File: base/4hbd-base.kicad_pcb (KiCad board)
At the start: 2 copper layers, 150 x 100 mm, 198 parts, among them J1 Screw_Terminal_01x03, J10 Conn_01x08, J12 Spring_Terminal_Connector_01x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, J14 Screw_Terminal_01x02, J15 Conn_01x27, J16 Conn_01x27, J2 Screw_Terminal_01x03, J3 Screw_Terminal_01x03, J4 Screw_Terminal_01x03, J5 Screw_Terminal_01x02, J6 Screw_Terminal_01x02, J7 Screw_Terminal_01x02, J8 Screw_Terminal_01x02, J9 Screw_Terminal_01x04, Q1 irf540n, Q10 2N7002, Q11 2N7002, Q12 IRLML2060TRPBF, Q2 irf540n, Q3 irf540n, Q4 irf540n, Q5 irf540n, Q6 irf540n, Q7 irf540n, Q8 irf540n, U1 SI8640, U11 MOCD217M, U12 MOCD217M, U13 MOCD217M, U14 AMS1117-5.0, U15 AMS1117-5.0, U16 LM2596S-ADJ, U17 AM26LV32, U18 LM2596S-ADJ, U19 AMS1117-5.0, U2 SI8640, U3 IR25606, U4 IR25606, U5 IR25606, U6 IR25606, U7 ACS712xLCTR-30A, U8 ACS712xLCTR-30A

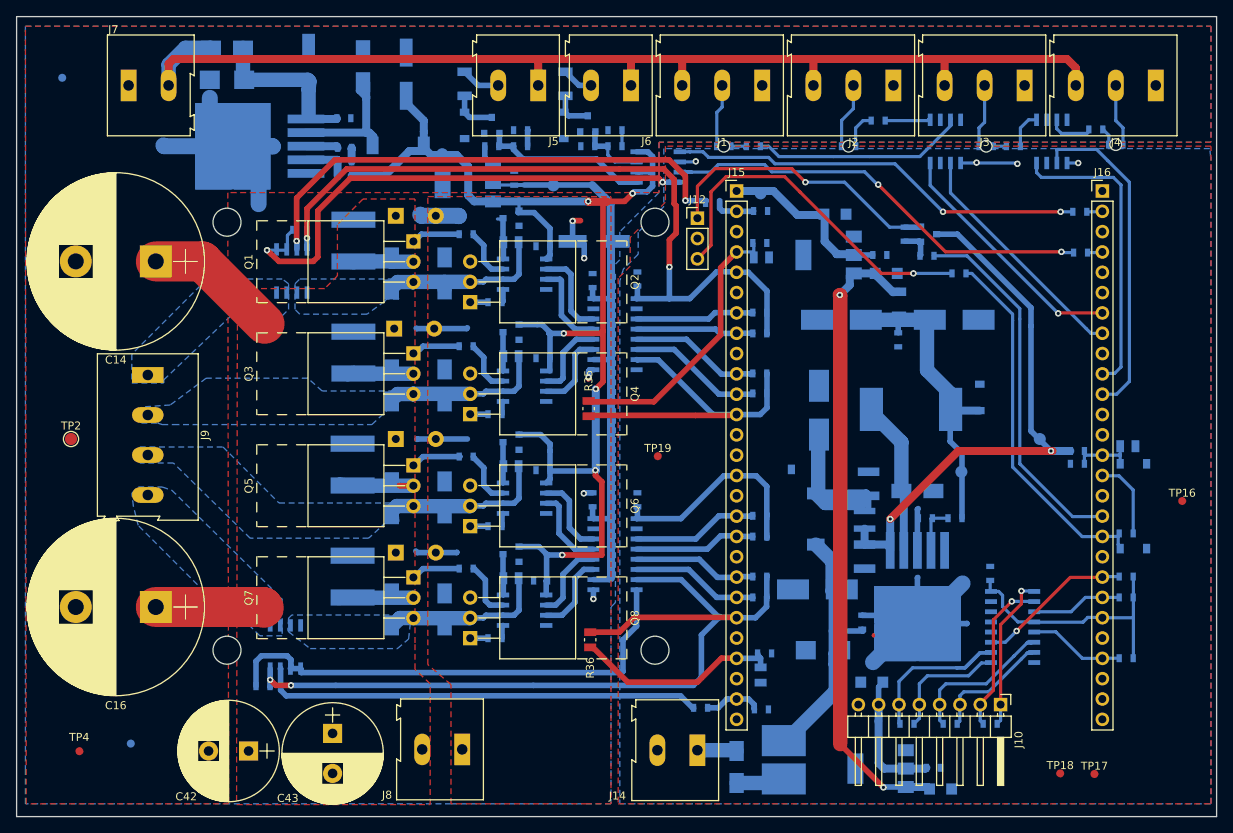
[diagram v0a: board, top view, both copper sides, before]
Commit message: add power vias
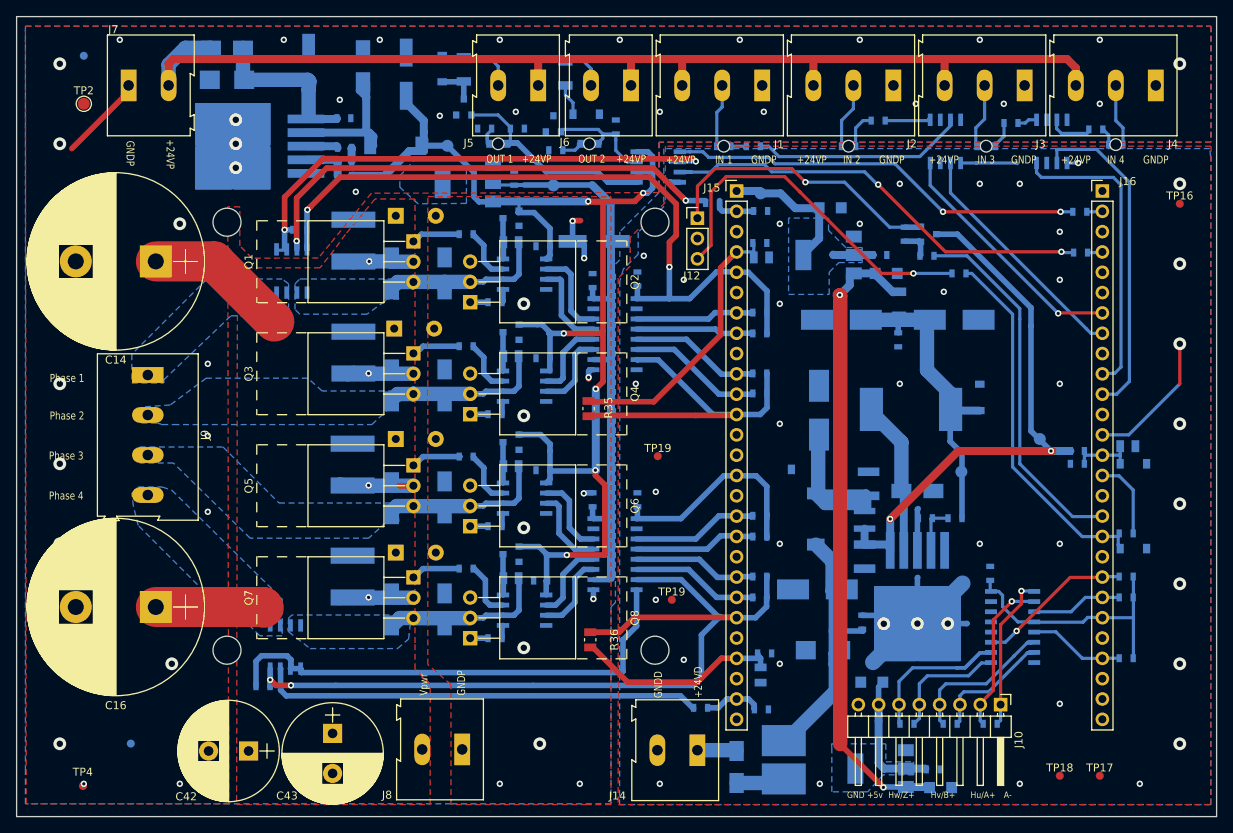
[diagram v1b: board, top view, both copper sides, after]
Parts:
- added TP19: GNDd, TestPoint:TestPoint_Pad_D1.5mm, F.Cu at (151.9, 135.9)
- D17, D18: footprint LED_SMD:LED_0603_1608Metric -> LED_SMD:LED_0603_1608Metric_ReverseMount
- moved TP2 41.9 mm to (78.4, 73.9)
- moved TP16 37.2 mm to (215.4, 86.4)
- moved R32 7.81 mm to (137.4, 79.7)
- moved D19 7.63 mm to (123.2, 69.5), turned to 90 degrees
- moved R31 4.50 mm to (128.5, 77.0)
- moved TP4 4.37 mm to (78.3, 159.2)
- moved Q11 4.30 mm to (137.1, 76.4)
- moved R34 4.24 mm to (144.9, 76.8), turned to 270 degrees
- moved Q10 4.19 mm to (125.9, 74.3)
- moved R33 3.88 mm to (132.6, 77.0), turned to 180 degrees
- moved TP1 3.85 mm to (78.4, 67.9)
- moved D18 3.21 mm to (141.6, 78.9), turned to 0 degrees
- moved D20 3.13 mm to (141.2, 75.2), turned to 0 degrees
- moved R29 2.92 mm to (194.3, 76.3)
- moved D17 2.82 mm to (130.2, 78.9), turned to 0 degrees
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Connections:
- U14 pad 4: (no net) -> /MCU/FPGA connection/+5V
- U15 pad 4: (no net) -> /Digital DC/DC/+5VEnc
- U19 pad 4: (no net) -> /MOSFETs/CurSense/Isolation/+5Vpwr
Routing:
- net GNDPWR: track 71.0 -> 26.2 mm, vias 5 -> 50
- net GND: track 183.0 -> 200.0 mm, vias 6 -> 41
- net Net-(D17-Pad2): track 21.2 -> 27.4 mm
- net Net-(D18-Pad2): track 8.47 -> 13.8 mm
- net /Encoder Interface/+3.3V: track 317.7 -> 313.1 mm
- net /MOSFETs/CurSense/Isolation/Vpwr: track 78.9 -> 82.6 mm, vias 0 -> 4
- net Net-(R17-Pad2): track 63.6 -> 60.8 mm
- net /DIO/DO0_P: track 4.91 -> 7.15 mm
- net Net-(R29-Pad1): track 4.72 -> 2.49 mm
- net /DIO/DO1_P: track 3.91 -> 5.67 mm
- net Net-(D15-Pad1): track 1.73 -> 3.43 mm
- net Net-(D20-Pad1): track 5.30 -> 3.99 mm
- net /MCU/FPGA connection/+5V: track 25.7 -> 26.6 mm
- net Net-(D19-Pad1): track 5.82 -> 4.91 mm
- net Net-(C5-Pad1): track 6.07 -> 5.37 mm
- added copper zone on B.Cu, net /Digital DC/DC/+5VEnc
- added copper zone on B.Cu, net /MCU/FPGA connection/+5V
- added copper zone on B.Cu, net /MOSFETs/CurSense/Isolation/+5Vpwr
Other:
- board text added: "+24VD"
- board text added: "+24VP"
- board text added: "+5v"
- board text added: "A-"
- board text added: "GND"
- board text added: "GNDD"
- board text added: "GNDP"
- board text added: "Hu/A+"
- board text added: "Hv/B+"
- board text added: "Hw/Z+"
- board text added: "IN 1"
- board text added: "IN 2"
- board text added: "IN 3"
- board text added: "IN 4"
- board text added: "OUT 1"
- board text added: "OUT 2"
- board text added: "Phase 1"
- board text added: "Phase 2"
- board text added: "Phase 3"
- board text added: "Phase 4"
- board text added: "Vpwr"

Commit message: generate gerber files
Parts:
- removed the TP19 at (151.9, 135.9)
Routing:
- net Net-(C22-Pad1): track 37.4 -> 34.5 mm
- net /DIO/+12V: track 173.2 -> 172.5 mm

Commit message: update gerbers
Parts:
- moved C49 0.20 mm to (117.4, 102.0)
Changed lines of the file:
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@@
     (links 447)
     (no_connects 16)
-    (area 69.924999 62.924999 220.075001 163.075001)
+    (area 58.214287 62.625 220.075001 163.3)
     (thickness 1.6)
     (drawings 50)
@@
   (page A4)
   (layers
-    (0 F.Cu mixed hide)
-    (31 B.Cu mixed)
+    (0 F.Cu mixed)
+    (31 B.Cu mixed hide)
     (32 B.Adhes user hide)
     (33 F.Adhes user hide)
@@
     (visible_elements FFFEFF7F)
     (pcbplotparams
-      (layerselection 0x00030_80000001)
+      (layerselection 0x010f0_80000001)
       (usegerberextensions false)
+      (gerberprecision 5)
       (excludeedgelayer true)
       (linewidth 0.100000)
@@
       (viasonmask false)
       (mode 1)
-      (useauxorigin false)
+      (useauxorigin true)
       (hpglpennumber 1)
       (hpglpenspeed 20)
@@
       (psa4output false)
       (plotreference true)
-      (plotvalue true)
+      (plotvalue false)
       (plotinvisibletext false)
       (padsonsilk false)
@@
       (outputformat 1)
       (mirror false)
-      (drillshape 1)
+      (drillshape 0)
       (scaleselection 1)
-      (outputdirectory ""))
+      (outputdirectory fab/))
   )
   (net 0 "")
@@
   )
   (module Capacitor_THT:CP_Radial_D10.0mm_P5.00mm (layer B.Cu)
-    (at 117.2 102)
+    (at 117.4 102)
     (descr "CP, Radial series, Radial, pin pitch=5.00mm, diameter=10mm, Electrolytic Capacitor")
     (tags "CP Radial series Radial pin pitch 5.00mm  diameter 10mm Electrolytic Capacitor")

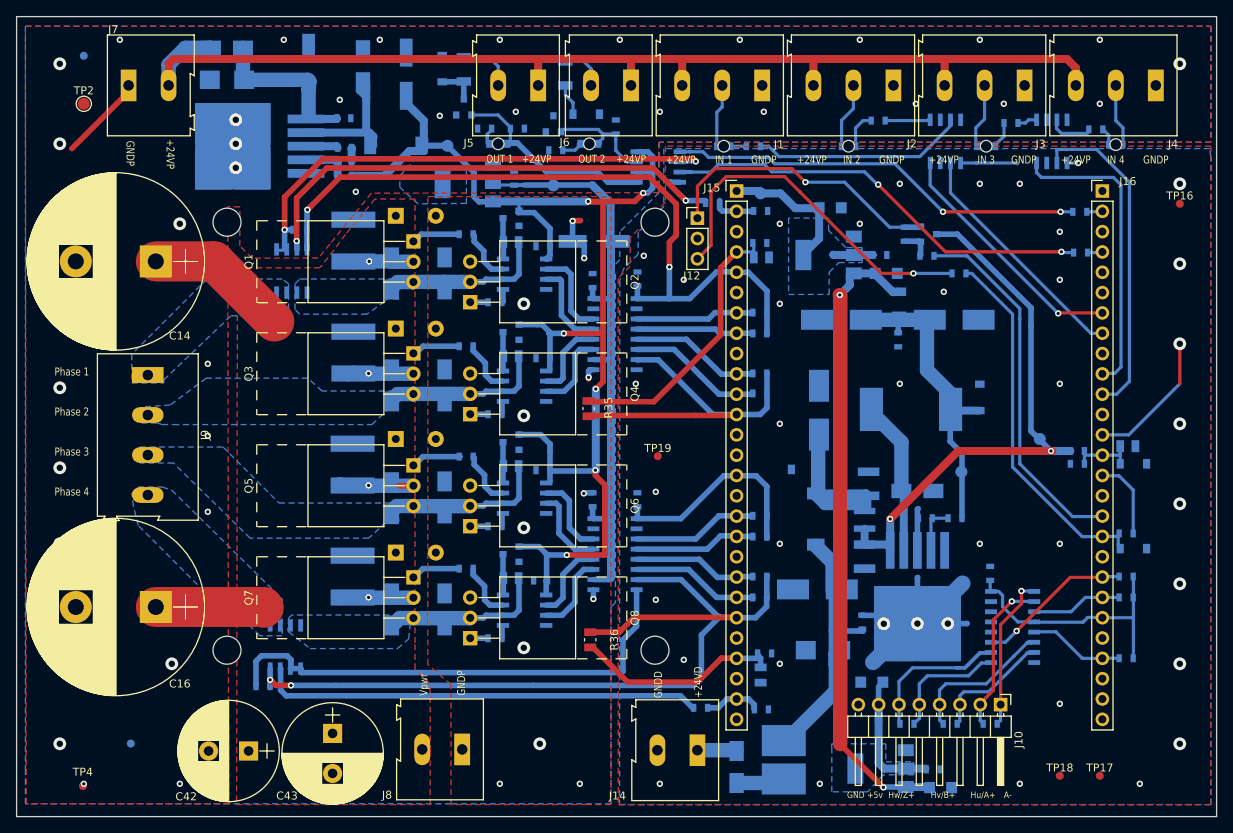
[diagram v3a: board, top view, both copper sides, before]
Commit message: fix vias lost netname by traces
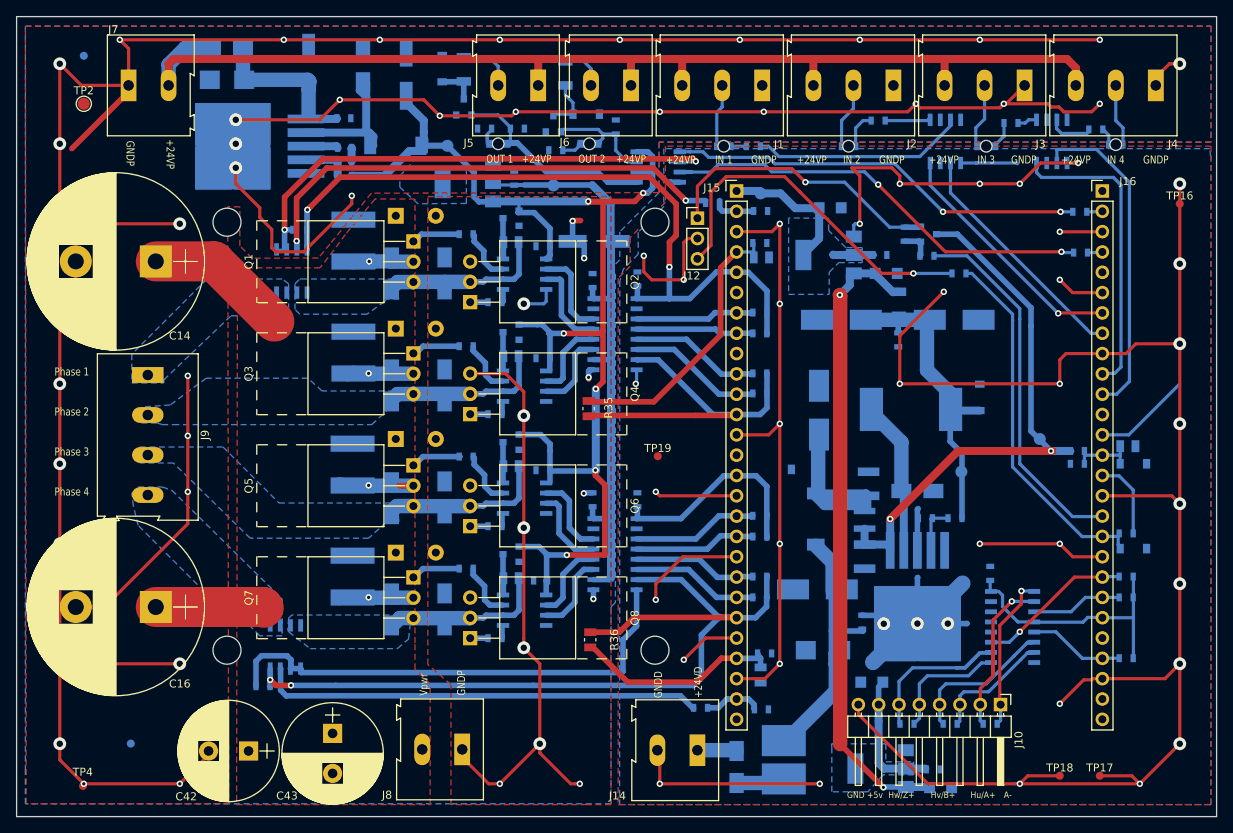
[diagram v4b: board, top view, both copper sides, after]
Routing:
- net GNDPWR: track 26.2 -> 560.6 mm
- net GND: track 200.0 -> 615.0 mm
- net /Encoder Interface/EncA+: track 20.3 -> 25.7 mm
- net Net-(D20-Pad1): track 3.99 -> 6.52 mm

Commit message: update poligone
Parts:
- C40, C41, C48, C49: footprint Capacitor_THT:CP_Radial_D10.0mm_P5.00mm -> Capacitor_THT:C_Disc_D7.5mm_W2.5mm_P5.00mm
- moved C40 0.40 mm to (117.4, 129.6)
- moved C49 0.40 mm to (117.4, 101.6)
- moved C41 0.20 mm to (117.4, 115.6)
- moved U12 0.10 mm to (186.1, 78.7)
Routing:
- net /MOSFETs/CurSense/Isolation/HB0: track 29.1 -> 41.3 mm
- net GND: track 615.0 -> 624.7 mm
- net GNDPWR: track 560.6 -> 567.7 mm
- net /Encoder Interface/+3.3V: track 313.1 -> 316.1 mm
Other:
- board text added: "!"
- board text added: "+"
